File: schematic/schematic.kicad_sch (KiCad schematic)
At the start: 89 parts, among them J1 GATE_OUT_1, J10 CV_OUT_2, J11 FWD_CLK_IN, J12 BWD_CLK_IN, J13 RST_IN, J14 KBD_Gate_Out, J2 GATE_OUT_2, J3 GATE_OUT_3, J4 GATE_OUT_4, J5 GATE_OUT_5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

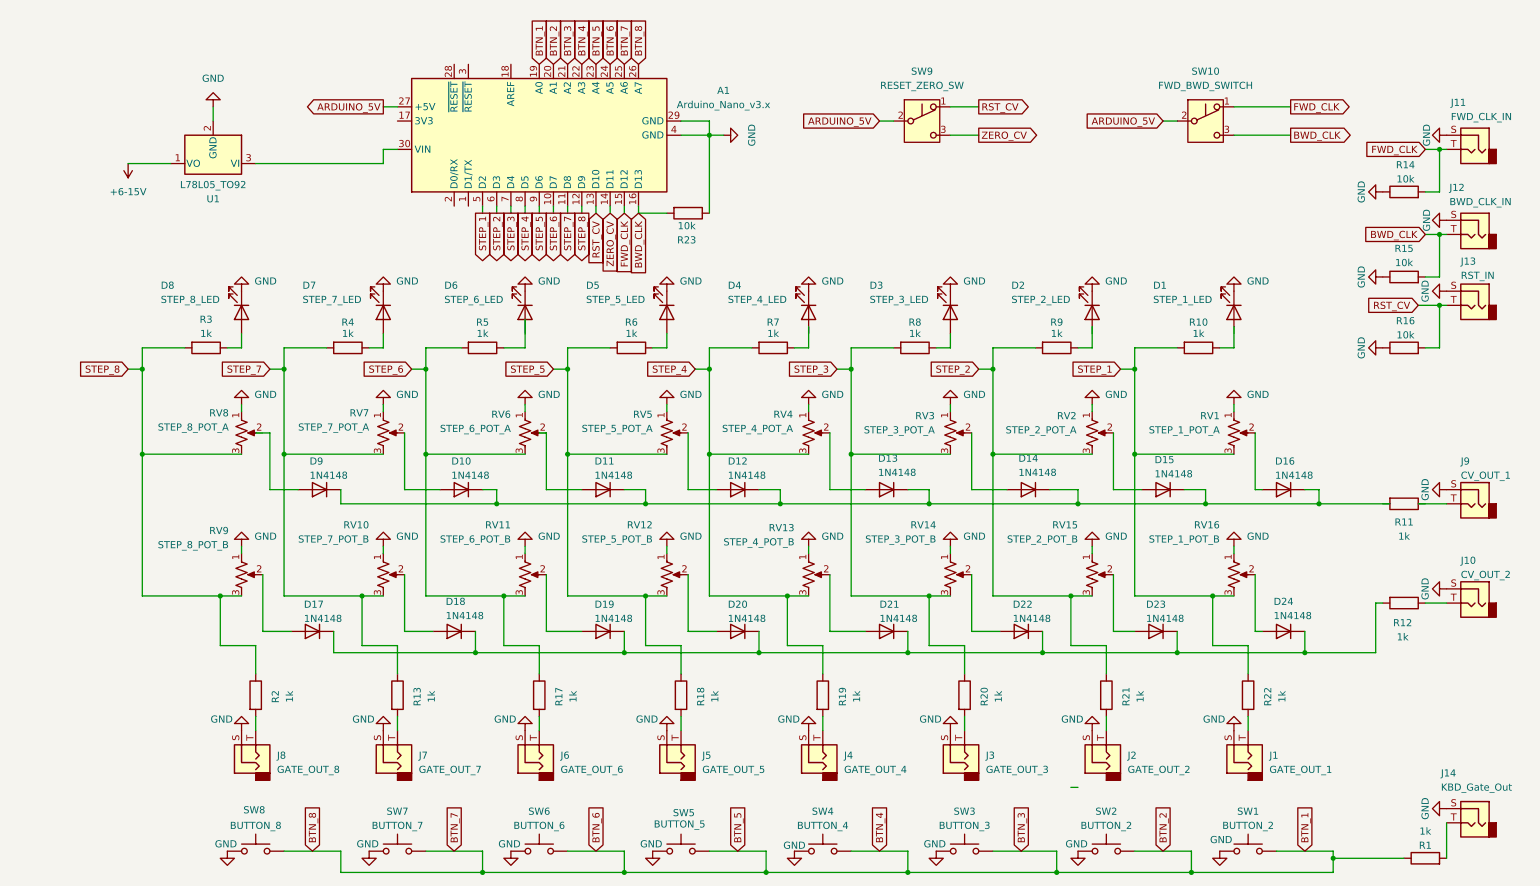
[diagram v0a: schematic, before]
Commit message: Fix pull ups and pull downs on schematic
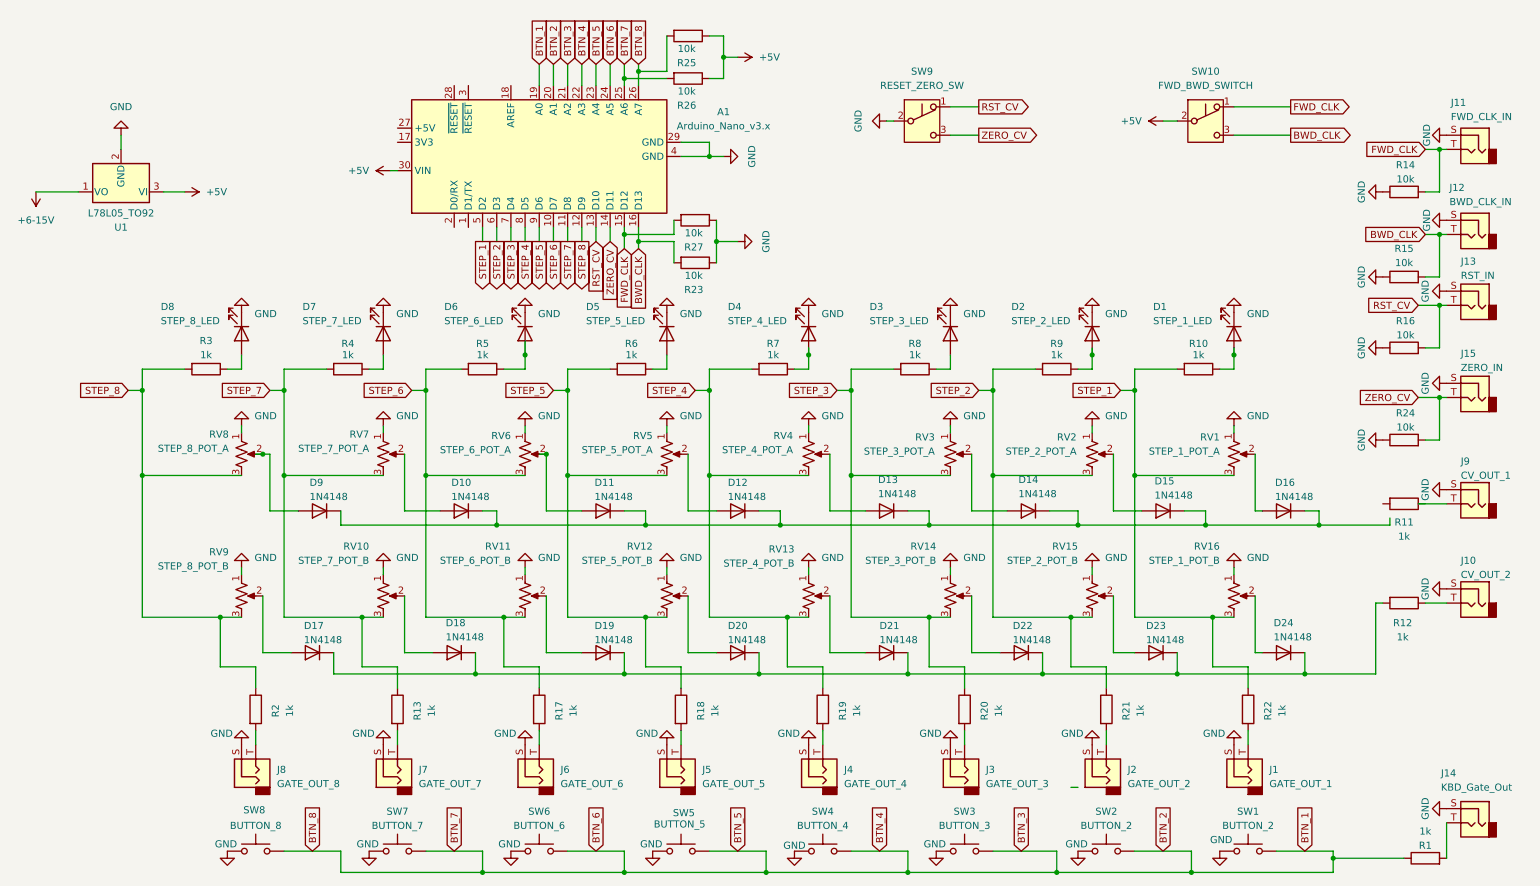
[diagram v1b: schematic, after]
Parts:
- added J15: ZERO_IN, symbol Connector_Audio:AudioJack2
- added R24, R25, R26, R27: 10k, symbol Device:R
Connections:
- net BTN_1: now also R25.2, R26.2
- net FWD_CLK: now also R27.2
- net GND: now also SW9.2 (B), J15.S, R24.1, R27.1
- net ZERO_CV: now also J15.T, R24.2
- net at R5.1: now also D6.2 (A)
- net at D1.2 (A): now also R10.1
- net at R7.1: now also D4.2 (A)
- net at D2.2 (A): now also R9.1
- net at D9.2 (A): now also RV8.2
- net +5V: now reaches A1.30 (VIN), U1.3 (VI)
- net +5V: now also SW10.2 (B), R25.1, R26.1
- removed net ARDUINO_5V: A1.27 (+5V), SW10.2 (B), SW9.2 (B)
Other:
- moved on the sheet: A1, D1, D10, D11, D12, D13, D14, D15, D16, D17, D18, D19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

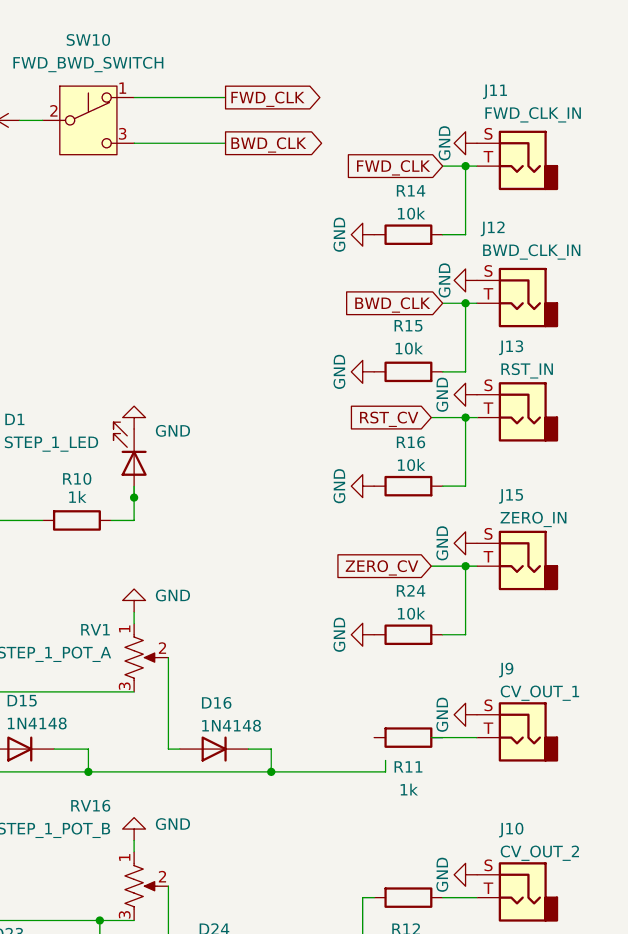
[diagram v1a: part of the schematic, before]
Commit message: Remove unnessesary (and wrong) resistors on FWD/BWD_CLK_IN
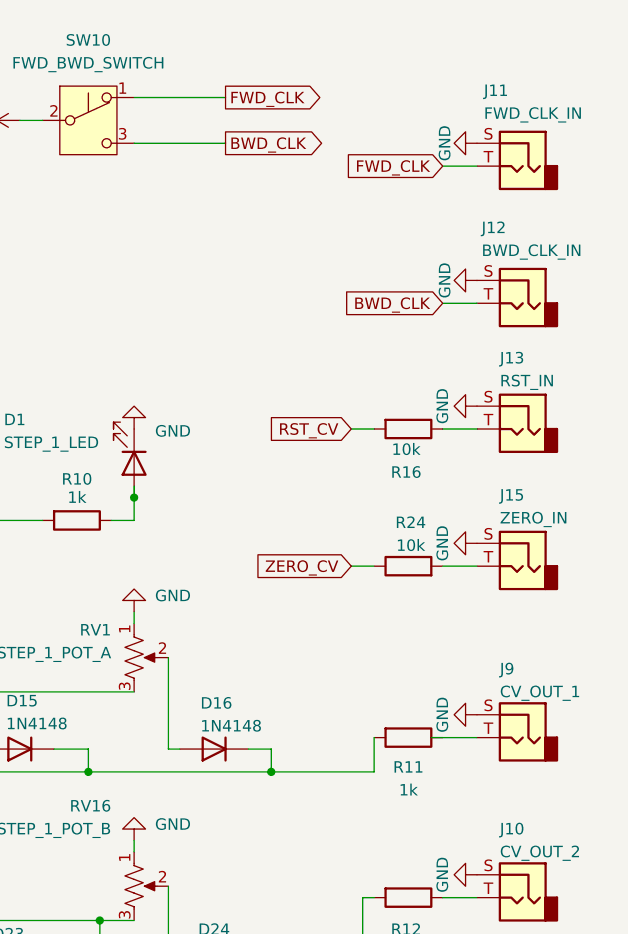
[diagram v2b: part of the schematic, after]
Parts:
- removed R14, R15: 10k, symbol Device:R
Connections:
- net GND: no longer R16.1, R24.1
- net RST_CV: no longer J13.T
- net ZERO_CV: now also R24.1; no longer J15.T, R24.2
- net at D10.1 (K), D11.1 (K), D12.1 (K)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: now also R11.2
- new net: J15.T, R24.2
- new net: J13.T, R16.1
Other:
- moved on the sheet: J13, R16, R24

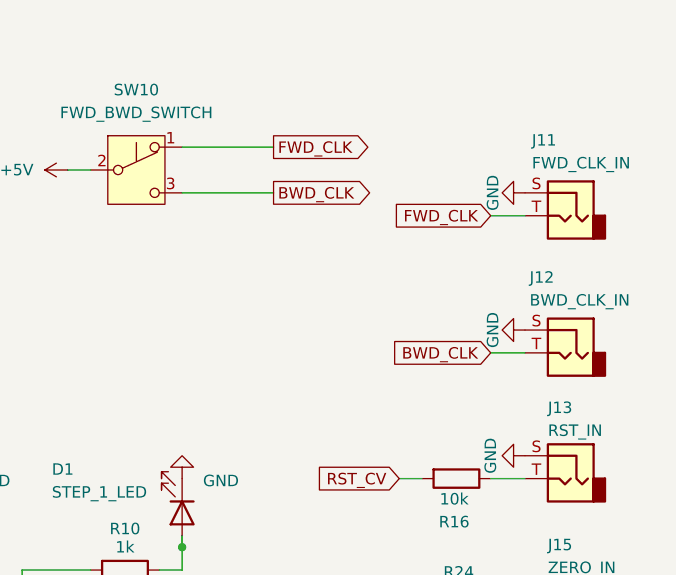
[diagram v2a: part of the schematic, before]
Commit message: Add diodes to FWD/BWD_CLK_IN
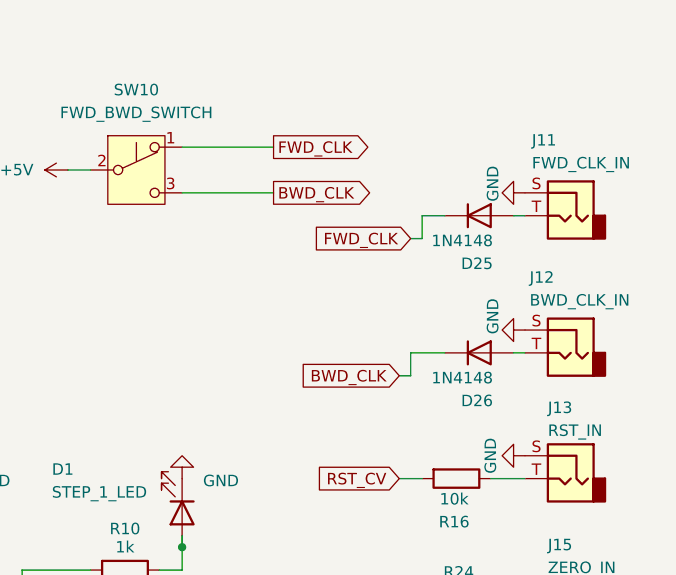
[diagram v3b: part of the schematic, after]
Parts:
- added D25, D26: 1N4148, Diode_THT:D_DO-35_SOD27_P7.62mm_Horizontal, symbol Diode:1N4148
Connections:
- net BWD_CLK: now also D26.1 (K); no longer J12.T
- net FWD_CLK: now also D25.1 (K); no longer J11.T
- new net: D25.2 (A), J11.T
- new net: D26.2 (A), J12.T
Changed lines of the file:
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@@
 	(wire
 		(pts
-			(xy 267.97 35.56) (xy 271.78 35.56)
+			(xy 259.08 38.1) (xy 260.35 38.1)
 		)
 		(stroke
@@
 	(wire
 		(pts
-			(xy 267.97 50.8) (xy 271.78 50.8)
-		)
-		(stroke
-			(width 0)
-			(type default)
-		)
-	)
-	(wire
-		(pts
 			(xy 182.88 86.36) (xy 182.88 85.09)
 		)
@@
 	(wire
 		(pts
+			(xy 259.08 50.8) (xy 259.08 53.34)
+		)
+		(stroke
+			(width 0)
+			(type default)
+		)
+	)
+	(wire
+		(pts
 			(xy 124.46 22.86) (xy 124.46 24.13)
 		)
@@
 	(wire
 		(pts
+			(xy 270.51 50.8) (xy 271.78 50.8)
+		)
+		(stroke
+			(width 0)
+			(type default)
+		)
+	)
+	(wire
+		(pts
 			(xy 165.1 93.98) (xy 165.1 119.38)
 		)
@@
 	(wire
 		(pts
+			(xy 260.35 35.56) (xy 262.89 35.56)
+		)
+		(stroke
+			(width 0)
+			(type default)
+		)
+	)
+	(wire
+		(pts
 			(xy 121.92 20.32) (xy 121.92 24.13)
 		)
@@
 	(wire
 		(pts
+			(xy 262.89 50.8) (xy 259.08 50.8)
+		)
+		(stroke
+			(width 0)
+			(type default)
+		)
+	)
+	(wire
+		(pts
 			(xy 179.07 102.87) (xy 205.74 102.87)
 		)
@@
 	(wire
 		(pts
+			(xy 257.81 53.34) (xy 259.08 53.34)
+		)
+		(stroke
+			(width 0)
+			(type default)
+		)
+	)
+	(wire
+		(pts
 			(xy 110.49 115.57) (xy 110.49 125.73)
 		)
@@
 	(wire
 		(pts
+			(xy 260.35 38.1) (xy 260.35 35.56)
+		)
+		(stroke
+			(width 0)
+			(type default)
+		)
+	)
+	(wire
+		(pts
 			(xy 127 49.53) (xy 127 52.07)
 		)
@@
 	(wire
 		(pts
+			(xy 270.51 35.56) (xy 271.78 35.56)
+		)
+		(stroke
+			(width 0)
+			(type default)
+		)
+	)
+	(wire
+		(pts
 			(xy 179.07 119.38) (xy 182.88 119.38)
 		)
@@
 	(global_label "BWD_CLK"
 		(shape input)
-		(at 267.97 50.8 180)
+		(at 257.81 53.34 180)
 		(fields_autoplaced yes)
 		(effects
@@
 		)
 		(property "Intersheetrefs" "${INTERSHEET_REFS}"
-			(at 256.4577 50.8 0)
+			(at 246.2977 53.34 0)
 			(effects
 				(font
@@
 	(global_label "FWD_CLK"
 		(shape input)
-		(at 267.97 35.56 180)
+		(at 259.08 38.1 180)
 		(fields_autoplaced yes)
 		(effects
@@
 		)
 		(property "Intersheetrefs" "${INTERSHEET_REFS}"
-			(at 256.6391 35.56 0)
+			(at 247.7491 38.1 0)
 			(effects
 				(font
@@
 		)
 		(property "Value" "GND"
-			(at 268.224 33.02 0)
+			(at 268.224 32.004 0)
 			(effects
 				(font
@@
 		)
 		(property "Value" "GND"
-			(at 268.224 48.26 0)
+			(at 268.224 46.736 0)
 			(effects
 				(font
@@
 	)
 	(symbol
+		(lib_id "Diode:1N4148")
+		(at 266.7 35.56 0)
+		(unit 1)
+		(exclude_from_sim no)
+		(in_bom yes)
+		(on_board yes)
+		(dnp no)
+		(property "Reference" "D25"
+			(at 268.224 40.894 0)
+			(effects
+				(font
+					(size 1.27 1.27)
+				)
+				(justify right)
+			)
+		)
+		(property "Value" "1N4148"
+			(at 268.224 38.354 0)
+			(effects
+				(font
+					(size 1.27 1.27)
+				)
+				(justify right)
+			)
+		)
+		(property "Footprint" "Diode_THT:D_DO-35_SOD27_P7.62mm_Horizontal"
+			(at 266.7 35.56 0)
+			(effects
+				(font
+					(size 1.27 1.27)
+				)
+				(hide yes)
+			)
+		)
+		(property "Datasheet" "https://assets.nexperia.com/documents/data-sheet/1N4148_1N4448.pdf"
+			(at 266.7 35.56 0)
+			(effects
+				(font
+					(size 1.27 1.27)
+				)
+				(hide yes)
+			)
+		)
+		(property "Description" "100V 0.15A standard switching diode, DO-35"
+			(at 266.7 35.56 0)
+			(effects
+				(font
+					(size 1.27 1.27)
+				)
+				(hide yes)
+			)
+		)
+		(property "Sim.Device" "D"
+			(at 266.7 35.56 0)
+			(effects
+				(font
+					(size 1.27 1.27)
+				)
+				(hide yes)
+			)
+		)
+		(property "Sim.Pins" "1=K 2=A"
+			(at 266.7 35.56 0)
+			(effects
+				(font
+					(size 1.27 1.27)
+				)
+				(hide yes)
+			)
+		)
+		(pin "1"
+		)
+		(pin "2"
+		)
+		(instances
+			(project "schematic"
+				(path "/17a4fd99-71a5-4ddc-81d0-959fe0ab5ae4"
+					(reference "D25")
+					(unit 1)
+				)
+			)
+		)
+	)
+	(symbol
 		(lib_id "power:GND")
 		(at 233.68 142.24 180)
@@
 					(unit 1)
 				)
+			)
+		)
+	)
+	(symbol
+		(lib_id "Diode:1N4148")
+		(at 266.7 50.8 0)
+		(unit 1)
+		(exclude_from_sim no)
+		(in_bom yes)
+		(on_board yes)
+		(dnp no)
+		(property "Reference" "D26"
+			(at 268.224 56.134 0)
+			(effects
+				(font
+					(size 1.27 1.27)
+				)
+				(justify right)
+			)
+		)
+		(property "Value" "1N4148"
+			(at 268.224 53.594 0)
+			(effects
+				(font
+					(size 1.27 1.27)
+				)
+				(justify right)
+			)
+		)
+		(property "Footprint" "Diode_THT:D_DO-35_SOD27_P7.62mm_Horizontal"
+			(at 266.7 50.8 0)
+			(effects
+				(font
+					(size 1.27 1.27)
+				)
+				(hide yes)
+			)
+		)
+		(property "Datasheet" "https://assets.nexperia.com/documents/data-sheet/1N4148_1N4448.pdf"
+			(at 266.7 50.8 0)
+			(effects
+				(font
+					(size 1.27 1.27)
+				)
+				(hide yes)
+			)
+		)
+		(property "Description" "100V 0.15A standard switching diode, DO-35"
+			(at 266.7 50.8 0)
+			(effects
+				(font
+					(size 1.27 1.27)
+				)
+				(hide yes)
+			)
+		)
+		(property "Sim.Device" "D"
+			(at 266.7 50.8 0)
+			(effects
+				(font
+					(size 1.27 1.27)
+				)
+				(hide yes)
+			)
+		)
+		(property "Sim.Pins" "1=K 2=A"
+			(at 266.7 50.8 0)
+			(effects
+				(font
+					(size 1.27 1.27)
+				)
+				(hide yes)
+			)
+		)
+		(pin "1"
+		)
+		(pin "2"
+		)
+		(instances
+			(project "schematic"
+				(path "/17a4fd99-71a5-4ddc-81d0-959fe0ab5ae4"
+					(reference "D26")
+					(unit 1)
+				)

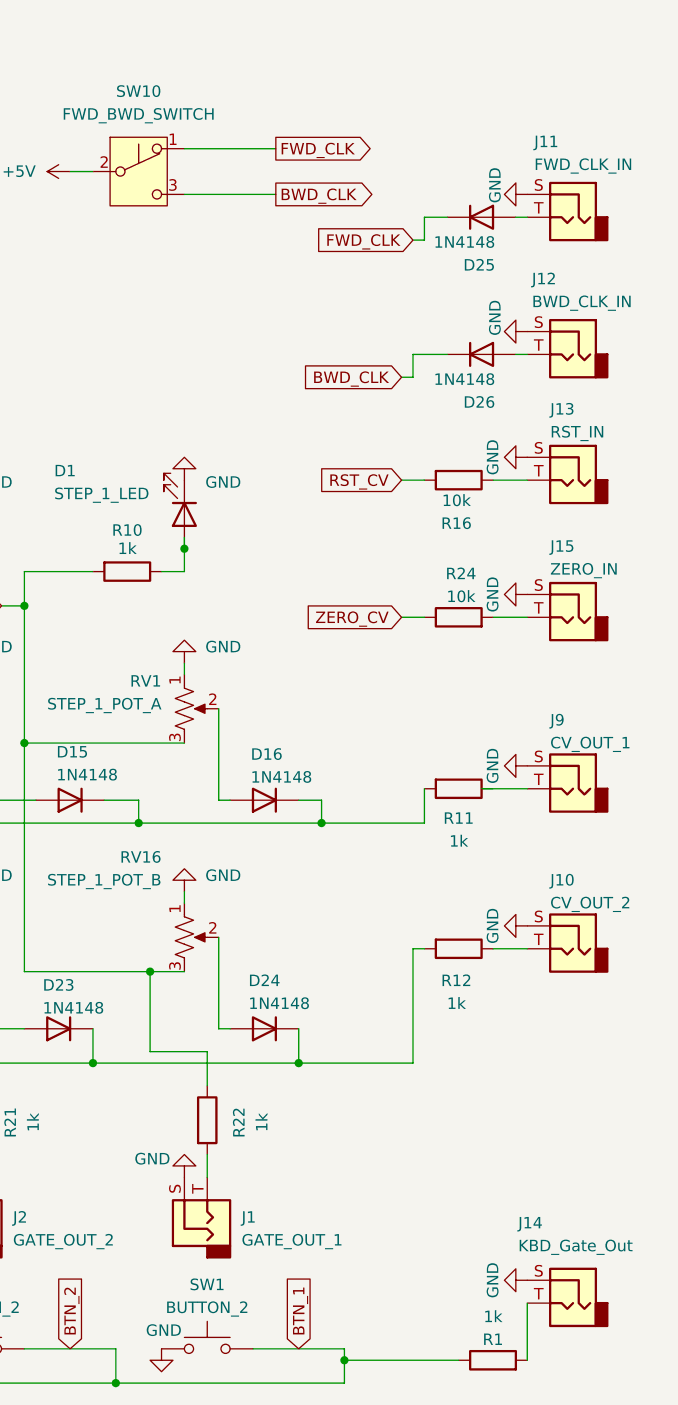
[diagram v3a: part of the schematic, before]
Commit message: Move diodes from FWD/BWD_CLK_IN to RST/ZERO_IN
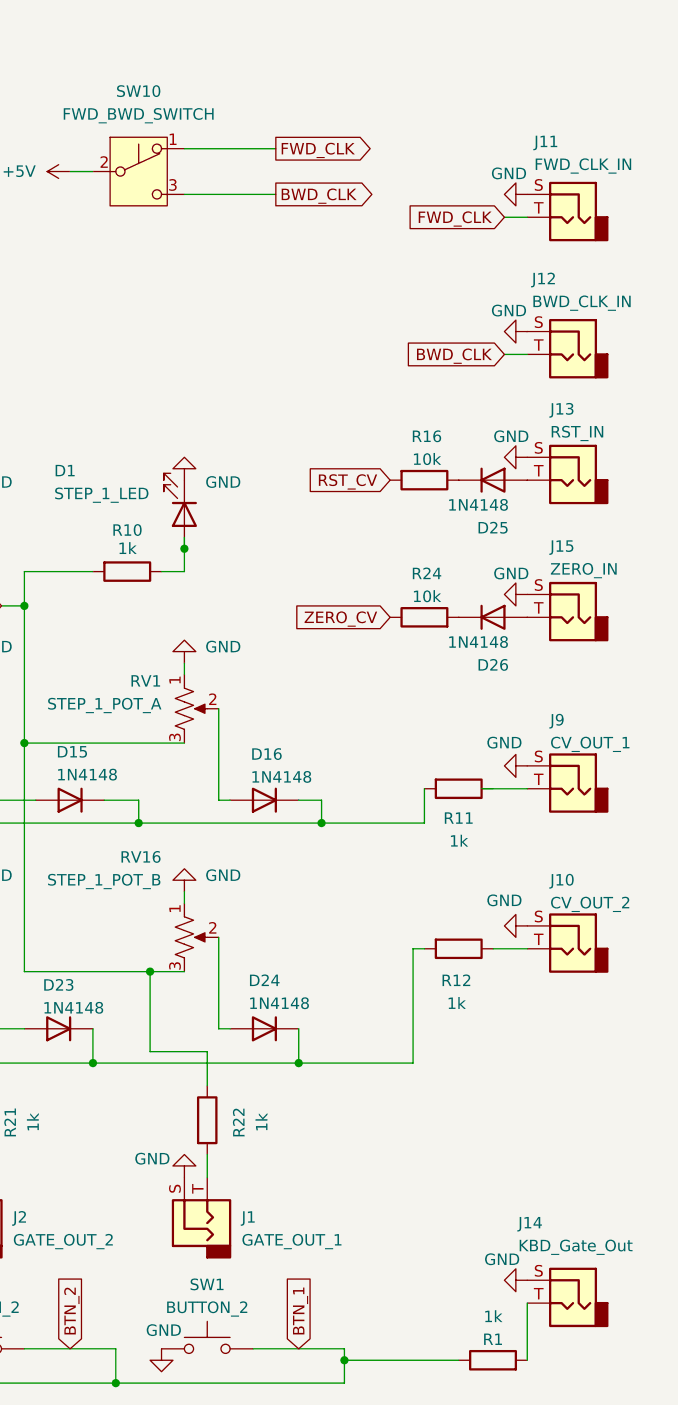
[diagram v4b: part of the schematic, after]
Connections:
- net BWD_CLK: now also J12.T; no longer D26.1 (K)
- net FWD_CLK: now also J11.T; no longer D25.1 (K)
- net at J15.T: now also D26.2 (A); no longer R24.2
- net at R16.1: now also D25.1 (K); no longer J13.T
- net at D25.2 (A): now also J13.T; no longer J11.T
- new net: D26.1 (K), R24.2
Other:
- moved on the sheet: R16, R24
